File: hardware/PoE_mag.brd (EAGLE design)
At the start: 149.9 x 124.5 mm, 124 parts, among them IC1 LD1117V33, IC10 PCA9517A, IC11 LD1117V33, IC2 DS1338, IC3 74LVC1T45SOT23-HAND, IC4 ATMEGA1284, IC5 MCP2200, IC6 TSR 1-2450, IC7 74LVC1T45SOT23-HAND, IC8 74LVC1T45SOT23-HAND, IC9 74LVC1T45SOT23-HAND, Q1 BSS138, Q3 BUK98150-55A, X1 PWR, X2 JTAG, X3 USB, X4 CONN-SMATHD, X5 UFL, X6 MICRO-SD-SOCKETHIROSE-DM3D, X7 RJ45, X8 RJ11, X9 22-23-2021, Y1 32k768, Y2 16MHz, Y3 12MHz

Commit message: Version before routing, and possible final routing
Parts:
- removed JP12: 5V LINK, SparkFun:1X02
- removed JP13: MAG VCC, SparkFun:1X03
- added JP2: ISP VCC, SparkFun:1X02
- added JP3: SQW, SparkFun:1X03
- C10: value 22p -> 4u7; device SteveMarple:0805-HAND -> SparkFun:CPOL-RADIAL-10UF-25V
- C11, C15, C16, C21, C22, C28: value 22p -> 100n; device SteveMarple:0805-HAND -> SteveMarple:1206-HAND
- C12, C33, C36: value 100n -> 1u
- C13: value 10n -> 22p; device SteveMarple:1206-HAND -> SteveMarple:0805-HAND
- C14, C19, C20, C34, C35: value 100n -> 22p; device SteveMarple:1206-HAND -> SteveMarple:0805-HAND
- C17: value 15p -> 10n; device SteveMarple:0805-HAND -> SteveMarple:1206-HAND
- C18: value 15p -> 100n; device SteveMarple:0805-HAND -> SteveMarple:1206-HAND
- C2: value 10u -> 1u; device SteveMarple:CPOL-RADIAL-10UF-25V -> SteveMarple:1206-HAND
- C27, C29, C39, C8: value 1u -> 100n
- C3: value 100n -> 10u; device SteveMarple:1206-HAND -> SteveMarple:CPOL-RADIAL-10UF-25V
- C31: value 1u -> 22p; device SteveMarple:1206-HAND -> SteveMarple:0805-HAND
- C32: value 4u7 -> 1u; device SteveMarple:CPOL-RADIAL-10UF-25V -> SteveMarple:1206-HAND
- C37: value 100n -> 4u7; device SteveMarple:1206-HAND -> SteveMarple:CPOL-RADIAL-10UF-25V
- C4: value 100p -> 15p; device SteveMarple:1206-HAND -> SteveMarple:0805-HAND
- C5: value 100n -> 15p; device SteveMarple:1206-HAND -> SteveMarple:0805-HAND
- C6: value 4u7 -> 100n; device SparkFun:CPOL-RADIAL-10UF-25V -> SteveMarple:1206-HAND
- C7: value 100n -> 100p
- D3: value BAS40 -> BAS21
- D4: value BAS21 -> BAS40
- IC1: device SteveMarple:TO220 -> SteveMarple:SOT223-HAND
- IC10: value PCA9517A -> 74LVC1T45SOT23-HAND; device SteveMarple:SO08 -> SteveMarple:SOT23-6-HAND
- IC11: value LD1117V33 -> PCA9517A; device SteveMarple:SOT223-HAND -> SteveMarple:SO08
- IC2: value DS1338 -> LD1117V33; device SteveMarple:SO08 -> SteveMarple:TO220
- IC3: value 74LVC1T45SOT23-HAND -> DS1338; device SteveMarple:SOT23-6-HAND -> SteveMarple:SO08
- IC5: value MCP2200 -> TSR 1-2450; device SteveMarple:SO20 -> PoE_lib:TSR-1-XXXX/POWERPAX-P78XX-10
- IC6: value TSR 1-2450 -> MCP2200; device PoE_lib:TSR-1-XXXX/POWERPAX-P78XX-10 -> SteveMarple:SO20
- JP1: value SQW -> 3V3/5V
- JP10: value CONFIG -> 5V LINK; device pinhead:2X05 -> SparkFun:1X02
- JP11: value GPS !RESET! (A0) -> MAG VCC; device SparkFun:1X02 -> SparkFun:1X03
- JP4: value PPS -> USB/VIN
- JP5: value 3V3/5V -> AUTO RST; device SparkFun:1X03 -> SparkFun:1X02
- JP6: value V ANT -> GPS !RESET! (A0); device SparkFun:1X03 -> SparkFun:1X02
- JP7: value AUTO RST -> V ANT; device SparkFun:1X02 -> SparkFun:1X03
- JP8: value ISP VCC -> CONFIG; device SparkFun:1X02 -> pinhead:2X05
- JP9: value USB/VIN -> PPS
- R10: value 1M -> 1k
- R18: value 3k 1% -> 330R
- R19: value 1k 1% -> 1M
- R20: value 1M -> 3k 1%
- R21: value 330R -> 1k 1%
- R3: value 10k -> 1M
- R4: value 4k7 -> 10k
- R6: value 10k -> 4k7
- R7: value 1k -> 10k
- U$5: value ? -> PAD
- U$8: value PAD -> ?
- X4: value CONN-SMATHD -> MICRO-SD-SOCKETHIROSE-DM3D; device SteveMarple:SMA-THD -> SteveMarple:MICRO-SD-SOCKET-HIROSE-DM3D
- X5: value UFL -> CONN-SMATHD; device SteveMarple:CONN-UFL-HAND-SOLDERING -> SteveMarple:SMA-THD
- X6: value MICRO-SD-SOCKETHIROSE-DM3D -> UFL; device SteveMarple:MICRO-SD-SOCKET-HIROSE-DM3D -> SteveMarple:CONN-UFL-HAND-SOLDERING
- X7: value RJ45 -> 22-23-2021; device SteveMarple:RJ45-8 -> con-molex:22-23-2021
- X8: value RJ11 -> RJ45; device SteveMarple:RJ11-6 -> SteveMarple:RJ45-8
- X9: value 22-23-2021 -> RJ11; device con-molex:22-23-2021 -> SteveMarple:RJ11-6
- moved X4 141.5 mm to (139.7, 66.0), turned to 90 degrees
- moved X6 136.7 mm to (15.2, 9.53), turned to 180 degrees
- moved D3 126.5 mm to (22.9, 86.4), turned to 270 degrees
- moved D4 126.5 mm to (129.5, 18.4), turned to 90 degrees
- moved R19 122.6 mm to (29.2, 95.2)
- moved R20 119.4 mm to (123.2, 21.6)
- moved IC3 105.4 mm to (141.0, 35.6), turned to 0 degrees
- moved R21 92.9 mm to (123.2, 16.5), turned to 0 degrees
- moved R18 89.4 mm to (57.1, 81.9), turned to 180 degrees
- moved JP7 89.0 mm to (2.54, 33.0), turned to 270 degrees
- moved C13 83.9 mm to (80.6, 87.6), turned to 180 degrees
- moved JP8 83.5 mm to (45.7, 39.4), turned to 0 degrees
- moved IC2 79.5 mm to (63.5, 17.8), turned to 90 degrees
- moved IC11 77.8 mm to (36.8, 74.9), turned to 90 degrees
- moved R3 75.3 mm to (64.8, 95.2), turned to 0 degrees
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- renumbered Q3 to Q2
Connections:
- net !GPS_RESET: now also IC7.3; no longer IC8.3
- net !MCP2200_RESET: now also IC6.4, R10.1; no longer IC5.4, R9.1
- net !RESET: now also C21.2, R7.1; no longer C12.2, R6.1
- net +3V3: now also C16.1, C3.1, C31.1, C32.1, C33.1, IC1.4, IC10.6, IC2.2, IC6.17, JP1.1, JP11.3, JP7.3, JP8.2, JP8.4, JP8.6, U$3.1; no longer C19.1, C2.1, C25.1, C35.1, C36.1, IC11.2, IC11.4, IC3.6, IC5.17, JP10.2, JP10.4, JP10.6, JP13.3, JP5.1, JP6.3, U$11.1
- net +5V: now also C2.1, IC2.3, JP1.3, JP10.1, JP4.2, JP7.1, U$4.1; no longer C39.1, IC11.3, JP12.1, JP5.3, JP6.1, JP9.2, U$12.1
- net +5V_USB: now also C17.1, JP4.3; no longer C13.1, JP9.3
- net 0(RX0): now also IC6.10; no longer IC5.10
- net 1(TX0): now also IC6.12; no longer IC5.12
- net 11(MOSI): now also X4.CMD; no longer X6.CMD
- net 12(MISO): now also X4.DAT0; no longer X6.DAT0
- net 13(SCK): now also R3.2, X4.CLK; no longer R10.2, X6.CLK
- net 15: now also JP3.1; no longer JP1.1
- net 20(SDA): now also IC11.3, IC3.5, R14.1, R6.1; no longer IC10.3, IC2.5, R15.1, R5.1
- net 21(SCL): now also IC11.2, IC3.6, R15.1, R5.1; no longer IC10.2, IC2.6, R14.1, R4.1
- net 22: now also X4.CD/DAT3; no longer X6.CD/DAT3
- net 3(TX1): now also IC8.4; no longer IC7.4
- net 6: now also JP3.3, JP9.3; no longer JP1.3, JP4.3
- net 7: now also JP9.1; no longer JP4.1
- net 8: now also R18.1; no longer R21.1
- net A0: now also JP6.1; no longer JP11.1
- net A2: now also D4.1, R20.2, R21.2; no longer D3.1, R18.2, R19.2
- net AREF: now also C8.1; no longer C5.1
- net AUTO_RESET: now also IC6.11, JP5.1; no longer IC5.11, JP7.1
- net AVCC: now also C11.1; no longer C9.1
- net FAN_CTRL: now also D3.3, X7.2; no longer D4.3, X9.2
- net GND: now also C12.2, D3.1, IC10.2, IC10.5, IC11.4, IC2.1, IC3.4, IC5.2@A, IC5.2@B, IC6.20, JP8.10, JP8.8, R21.1, R3.1, U$2.1, X4.GND, X4.SHIELD@0, X5.GND@2, X5.GND@3, X6.GND@0, X6.GND@1, X8.4, X9.2, X9.3; no longer C34.2, D4.1, IC10.4, IC11.1, IC2.4, IC3.2, IC3.5, IC5.20, IC6.2@A, IC6.2@B, JP10.10, JP10.8, R10.1, R20.1, U$13.1, X4.GND@0, X4.GND@1, X4.GND@2, X4.GND@3, X6.GND, X6.SHIELD@0, X7.3, X7.4, X8.2
- net GPIO0: now also U$6.1; no longer U$3.1
- net GPIO1: now also IC10.4, U$7.1; no longer IC9.4, U$4.1
- net GPIO2: now also U$8.1; no longer U$5.1
- net GPIO3: now also JP8.1, U$9.1; no longer JP10.1, U$6.1
- net GPIO4: now also JP8.3, U$10.1; no longer JP10.3, U$7.1
- net GPIO5: now also JP8.5, U$11.1; no longer JP10.5, U$8.1
- net GPIO6: now also JP8.7, U$12.1; no longer JP10.7, U$9.1
- net GPIO7: now also JP8.9, U$13.1; no longer JP10.9, U$10.1
- net GPS_RX1: now also IC8.3; no longer IC7.3
- net GPS_TX1: now also IC9.4; no longer IC3.4
- net MAG_SCL: now also IC11.7, X8.5, X9.4; no longer IC10.7, X7.5, X8.4
- net MAG_SDA: now also IC11.6, X8.7, X9.6; no longer IC10.6, X7.7, X8.6
- net MAG_VCC: now also C39.1, IC11.5, IC11.8, JP10.2, X8.6, X9.5; no longer C37.1, IC10.5, IC10.8, JP12.2, X7.6, X8.5
- net N$1: now also C14.1; no longer C11.1
- net N$11: now also C7.1, IC3.3, R9.2; no longer C4.1, IC2.3, R7.2
- net N$12: now also C5.1, IC3.2; no longer C17.1, IC2.2
- net N$14: now also IC5.3@A, IC5.3@B, JP4.1; no longer IC6.3@A, IC6.3@B, JP9.1
- net N$15: now also C21.1, JP5.2; no longer C12.1, JP7.2
- net N$18: now also C19.1, IC6.2; no longer C15.1, IC5.2
- net N$2: now also C13.1; no longer C10.1
- net N$22: now also IC7.4, JP6.2; no longer IC8.4, JP11.2
- net N$23: now also C34.2, X5.SIG, X6.SIGNAL; no longer C21.2, X4.SIG, X5.SIGNAL
- net N$24: now also C34.1; no longer C21.1
- net N$25: now also IC9.3; no longer IC3.3
- net N$26: now also JP11.2, X8.8; no longer JP13.2, X7.8
- net N$29: now also R18.2, R19.2; no longer R20.2, R21.2
- net N$5: now also C4.1, IC3.1; no longer C18.1, IC2.1
- net N$6: now also JP2.1; no longer JP8.1
- net N$7: now also C20.1, IC6.3; no longer C16.1, IC5.3
- net N$9: now also R9.1; no longer R7.1
- net PPS: now also IC10.3, JP9.2; no longer IC9.3, JP4.2
- net SLEEP_FLAG: now also U$5.1; no longer U$2.1
- net SQW: now also IC3.7, JP3.2, R4.1; no longer IC2.7, JP1.2, R3.1
- net USB_D+: now also IC6.19; no longer IC5.19
- net USB_D-: now also IC6.18; no longer IC5.18
- net VCC: now also C10.1, C15.1, C18.1, C22.1, C25.1, C9.1, D4.3, IC11.1, IC3.8, IC6.1, JP1.2, JP2.2, R10.2, R7.2, X4.VDD; no longer C14.1, C20.1, C3.1, C33.1, C34.1, C7.1, D3.3, IC2.8, IC3.1, IC5.1, JP5.2, JP8.2, R3.2, R9.2, X6.VDD
- net VIN: now also C12.1, IC5.1@A, IC5.1@B, JP11.1, R20.1, X7.1, X8.2; no longer C8.1, IC6.1@A, IC6.1@B, JP13.1, R18.1, X7.2, X8.1
- net V_ANT: now also C35.1, C36.1, C37.1, JP7.2; no longer C22.1, C31.1, C32.1, JP6.2
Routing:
- net GND: track 242.6 -> 1151.1 mm, vias 27 -> 34
- net VCC: track 40.5 -> 452.7 mm, vias 0 -> 8
- net +3V3: track 43.5 -> 349.7 mm, vias 0 -> 4
- net VIN: track 0.00 -> 283.4 mm, vias 0 -> 1
- net 20(SDA): track 0.00 -> 219.8 mm, vias 0 -> 3
- net 21(SCL): track 0.00 -> 208.7 mm, vias 0 -> 4
- net !RESET: track 0.00 -> 192.1 mm, vias 0 -> 4
- net 1(TX0): track 0.00 -> 192.0 mm, vias 0 -> 2
- net 2(RX1): track 0.00 -> 158.0 mm, vias 0 -> 4
- net +5V: track 9.52 -> 164.1 mm, vias 0 -> 1
- net 3(TX1): track 0.00 -> 140.2 mm, vias 0 -> 2
- net 0(RX0): track 0.00 -> 136.5 mm, vias 0 -> 3
- net 18(TMS): track 0.00 -> 125.3 mm
- net VBATT: track 0.00 -> 123.9 mm, vias 0 -> 1
- net 22: track 0.00 -> 121.5 mm
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
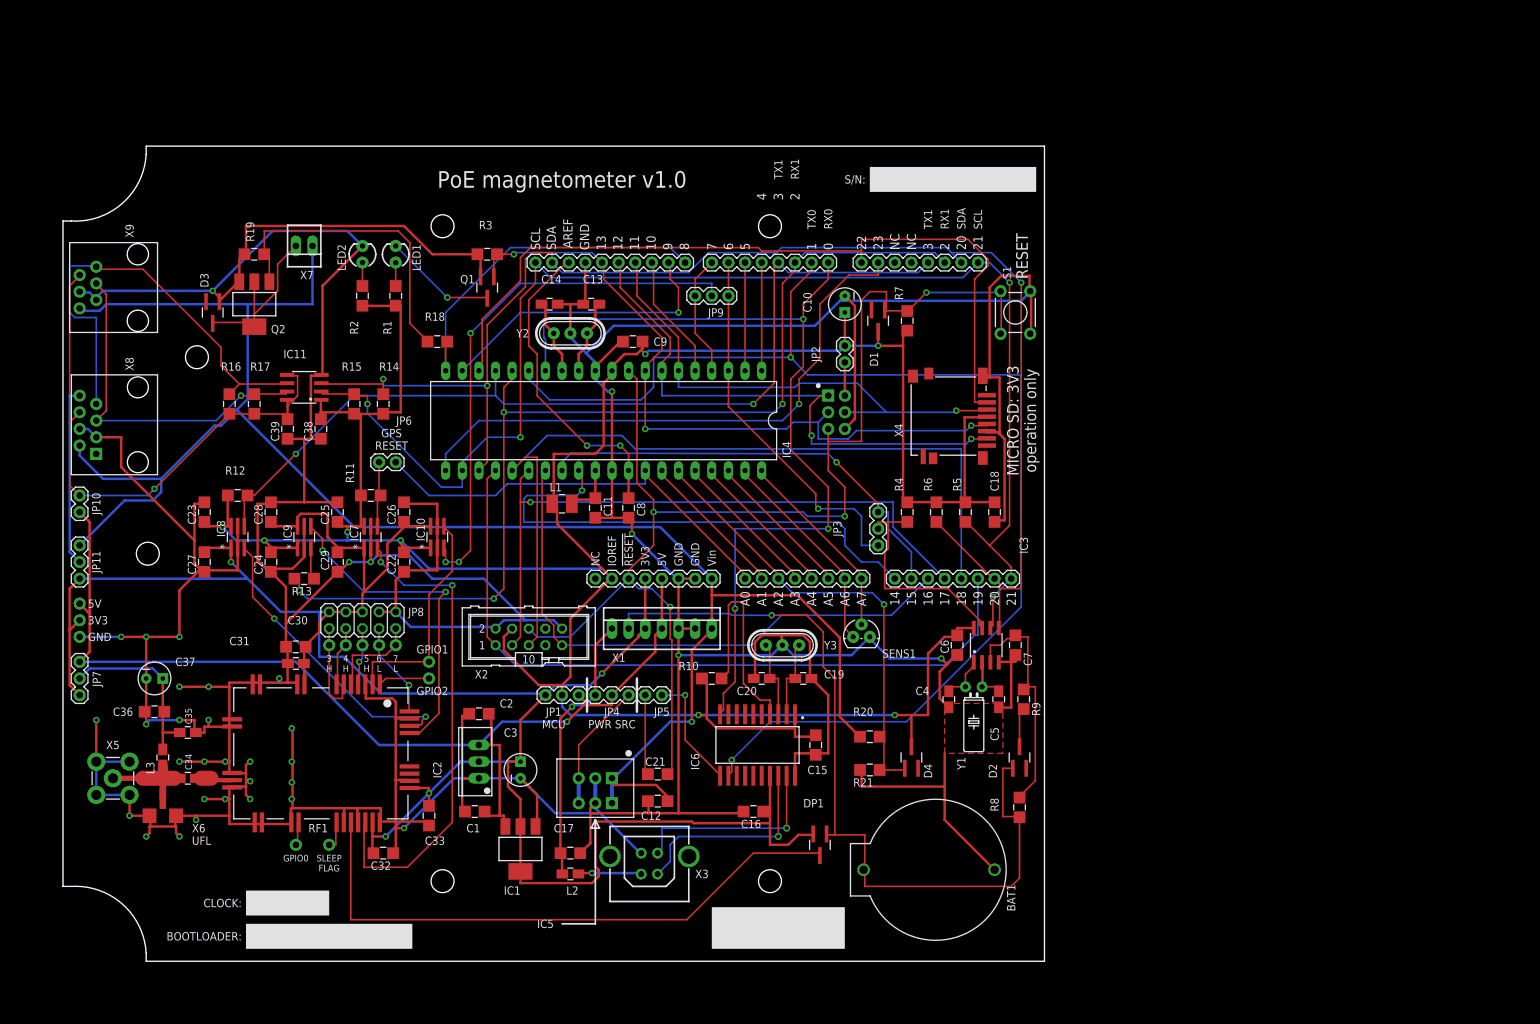
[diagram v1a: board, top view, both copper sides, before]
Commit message: Improve layout and track spacing
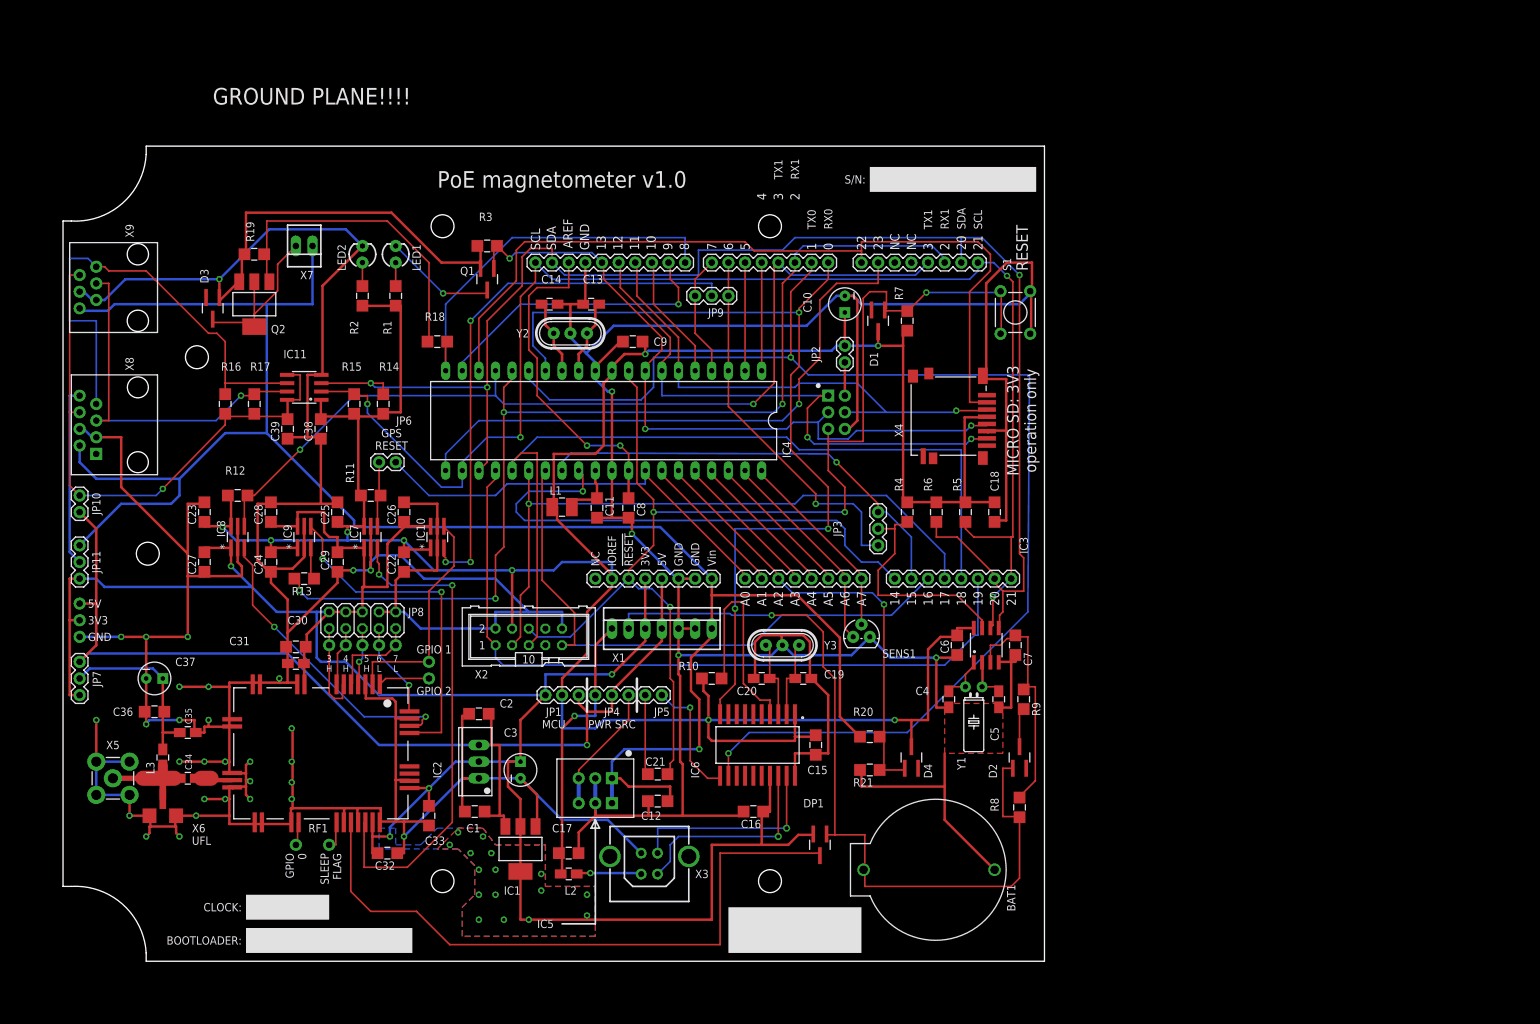
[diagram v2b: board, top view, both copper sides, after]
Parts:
- moved Q1 1.27 mm to (64.8, 91.4)
- moved R3 1.27 mm to (64.8, 96.5)
- moved D3 0.64 mm to (22.9, 87.0)
- moved C32 0.63 mm to (49.5, 3.81)
- moved R16 0.63 mm to (24.8, 72.4)
- moved L1 0.51 mm to (76.2, 56.6)
- moved C11 0.25 mm to (81.5, 56.5)
- moved C17 0.25 mm to (77.2, 3.81)
- moved L2 0.25 mm to (77.2, 0.64)
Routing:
- net GND: track 1151.1 -> 1181.4 mm
- net +3V3: track 349.7 -> 367.7 mm, vias 4 -> 20
- net 20(SDA): track 219.8 -> 230.4 mm
- net VIN: track 283.4 -> 293.5 mm
- net V_BACKUP: track 91.2 -> 100.0 mm
- net +5V: track 164.1 -> 171.1 mm
- net 8: track 55.1 -> 59.3 mm
- net 1(TX0): track 192.0 -> 195.6 mm
- net VCC: track 452.7 -> 456.2 mm, vias 8 -> 9
- net 22: track 121.5 -> 124.8 mm
- net MAG_SDA: track 69.5 -> 72.8 mm
- net 21(SCL): track 208.7 -> 211.5 mm
- net MAG_SCL: track 53.5 -> 56.3 mm
- net 0(RX0): track 136.5 -> 139.2 mm
- net 16(TDI): track 88.2 -> 90.9 mm
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- added copper zone on layer 1, net +3V3
- added copper zone on layer 16, net +3V3
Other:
- board text added: "GPIO 0"
- board text added: "GPIO 1"
- board text added: "GPIO 2"
- board text added: "GROUND PLANE!!!!"
- board text removed: "GPIO0"
- board text removed: "GPIO1"
- board text removed: "GPIO2"

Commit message: Fix incorrect USB power filtering
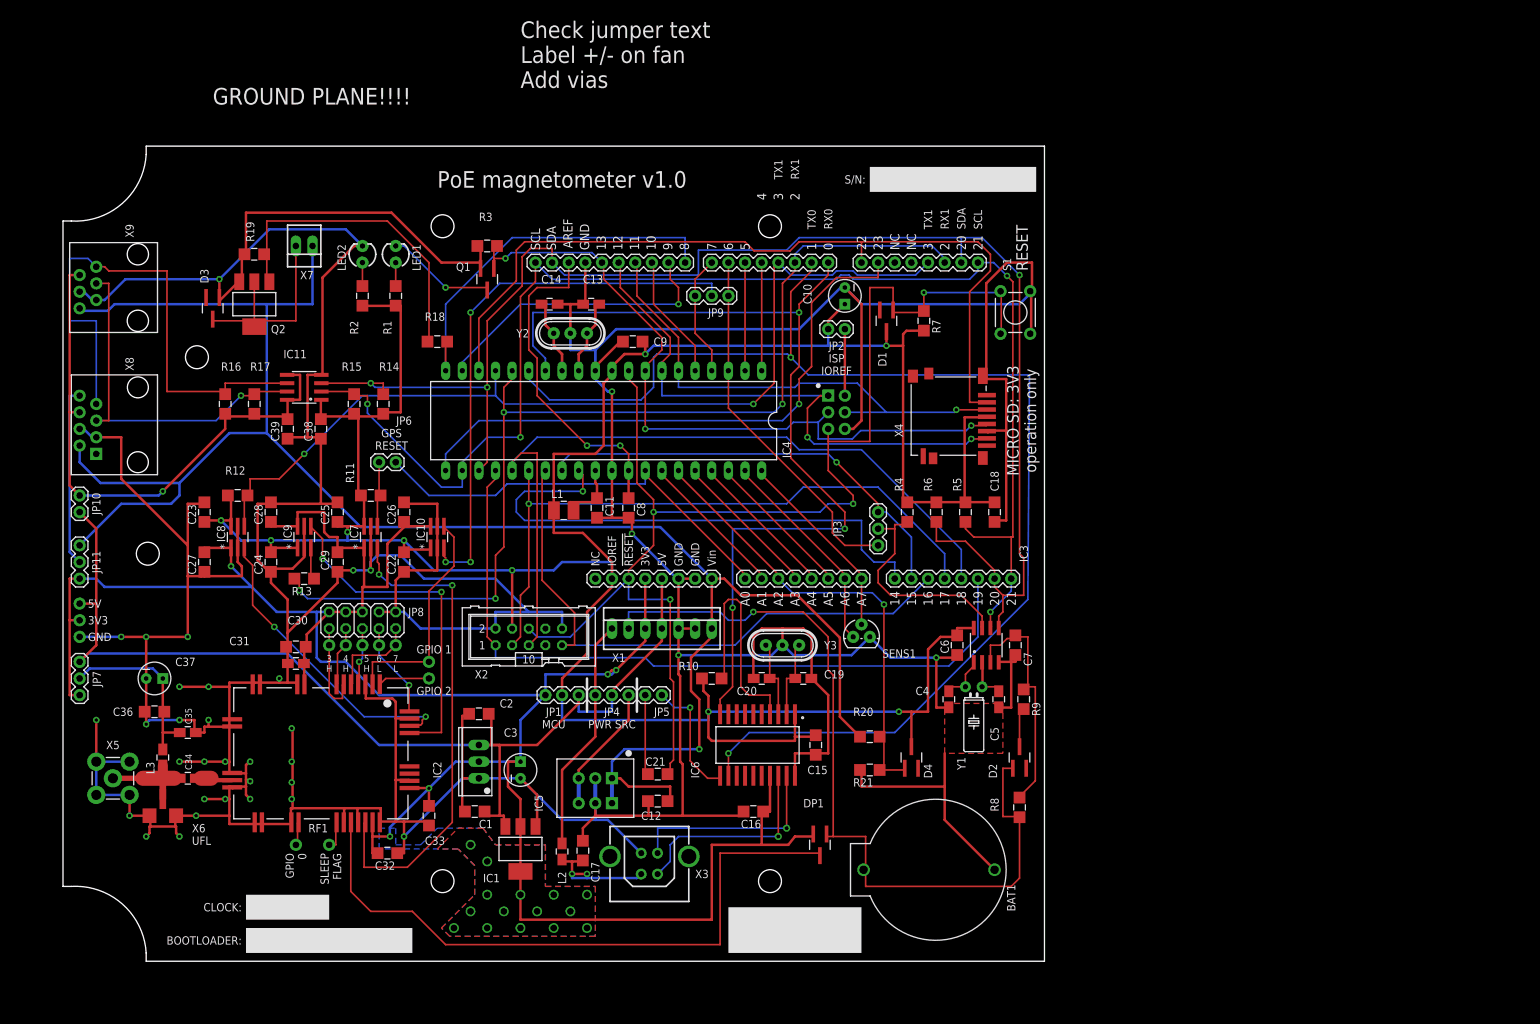
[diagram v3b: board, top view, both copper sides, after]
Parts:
- JP2: value ISP VCC -> ISP IOREF
- moved JP2 5.08 mm to (119.4, 83.8), turned to 180 degrees
- moved L2 3.58 mm to (76.2, 4.06), turned to 90 degrees
- moved R7 2.54 mm to (131.4, 85.1)
- moved C17 2.19 mm to (79.4, 4.19), turned to 90 degrees
- moved C10 1.27 mm to (119.4, 88.9)
- moved D1 1.27 mm to (125.7, 85.1)
- moved L1 0.57 mm to (76.5, 56.1)
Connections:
- net +5V_USB: no longer C17.1
- net VBUS: now also C17.1
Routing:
- net VBUS: track 9.93 -> 19.9 mm, vias 1 -> 2
- net 18(TMS): track 127.4 -> 118.5 mm
- net MAG_SDA: track 72.8 -> 80.4 mm
- net VCC: track 456.2 -> 463.7 mm
- net +5V_USB: track 43.2 -> 36.0 mm, vias 1 -> 0
- net !RESET: track 191.8 -> 198.8 mm
- net N$6: track 5.08 -> 10.2 mm
- net FAN_CTRL: track 26.9 -> 31.4 mm
- net 0(RX0): track 139.2 -> 143.0 mm
- net 14: track 79.1 -> 82.1 mm
- net GND: track 1181.4 -> 1184.4 mm
- net 3(TX1): track 140.5 -> 142.5 mm
- net 6: track 57.5 -> 55.6 mm, vias 1 -> 0
- net +3V3: track 367.7 -> 369.5 mm
- net +5V: track 171.1 -> 169.4 mm, vias 1 -> 0
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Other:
- board text added: "+ -"
- board text added: "Check jumper text Label +/- on fan Add vias"
- board text added: "ISP IOREF"

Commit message: Routed layout with no DRC warnings
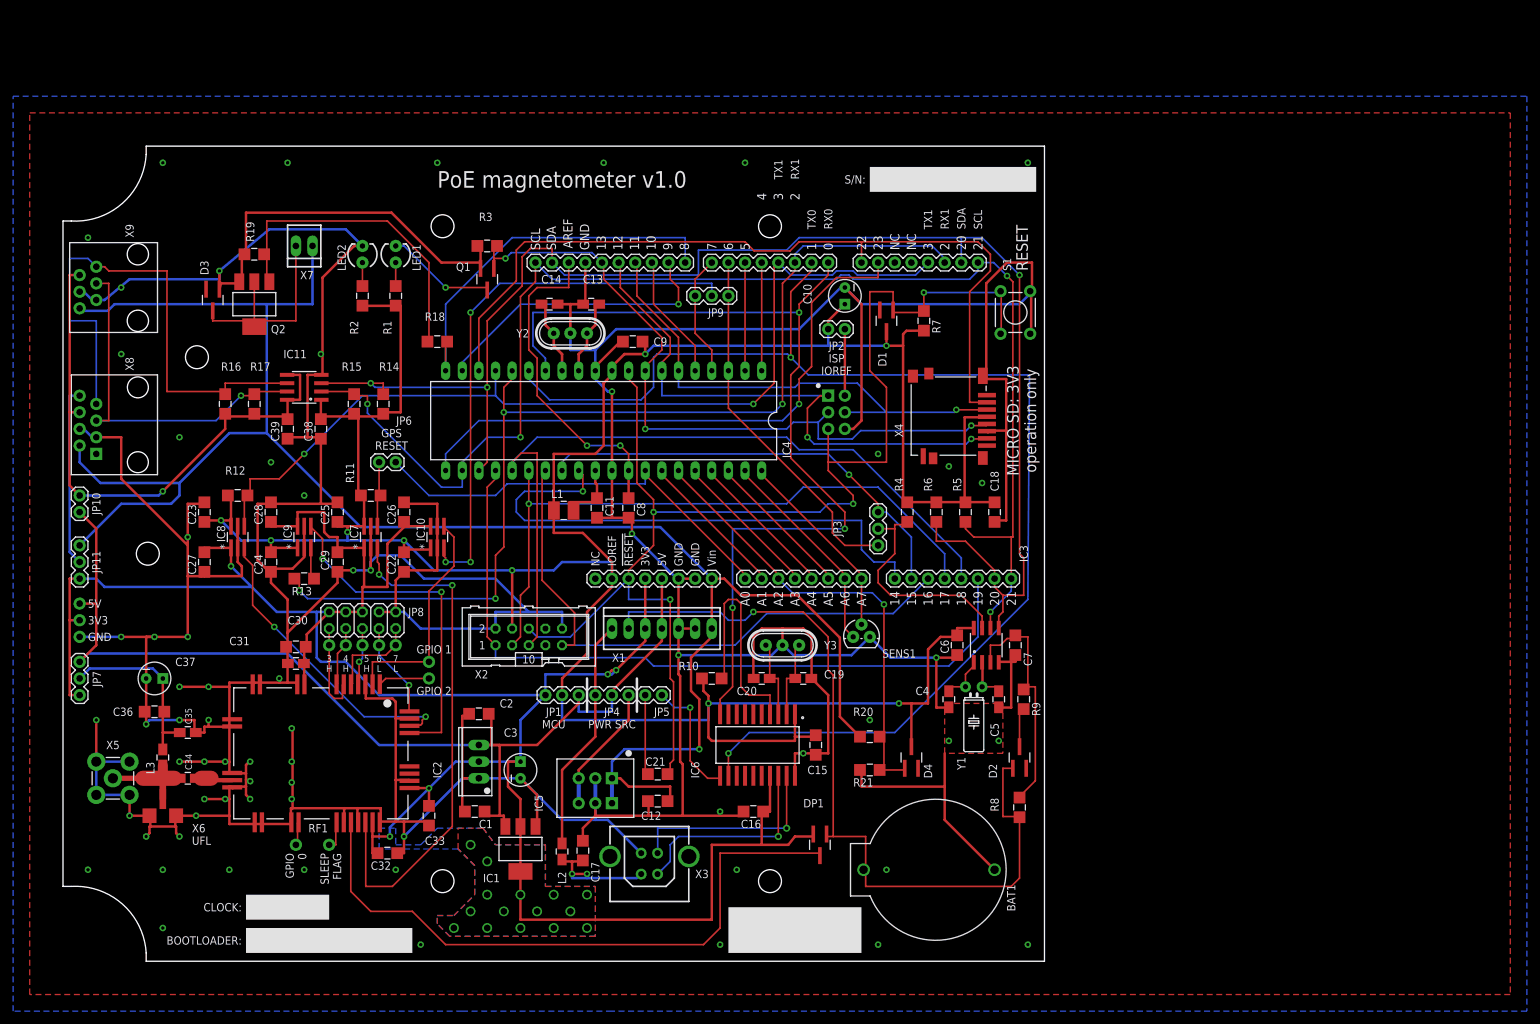
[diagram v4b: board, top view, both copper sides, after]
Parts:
- LED1, LED2: device SparkFun:LED3MM -> PoE_lib:LED3MM
- X1: device con-molex:22-23-2071 -> PoE_lib:22-23-2071
- X7: device con-molex:22-23-2021 -> PoE_lib:22-23-2021
- moved D3 1.27 mm to (22.9, 88.3)
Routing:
- net !RESET: track 198.8 -> 204.3 mm
- net !GPS_RESET: track 75.4 -> 79.6 mm
- net V_BACKUP: track 100.0 -> 98.5 mm
- net VCC: track 463.7 -> 465.0 mm
- net FAN_CTRL: track 31.4 -> 32.6 mm
- net 18(TMS): track 118.5 -> 117.8 mm
- net GND: track 1184.4 -> 1185.0 mm, vias 34 -> 68
- added copper zone on layer 16, net GND
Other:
- board text removed: "Check jumper text Label +/- on fan Add vias"
- board text removed: "GROUND PLANE!!!!"
